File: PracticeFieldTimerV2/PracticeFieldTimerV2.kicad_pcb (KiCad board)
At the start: 2 copper layers, 106 x 153 mm, 43 parts, among them J1 External Controls, J3 Panel, J5 /CAN Enable, J6 RJ45-B, J7 RJ45-A, J8 CAN Terminate, U1 ESP32-DevKitC, U2 PCF8574N, U3 20 x 4 LCD, U4 DS3231MZ_TRL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

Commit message: Fix reversed power and ground on LCD backlight LED.
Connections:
- U3 pad 15: GND -> +3.3V
- U3 pad 16: +3.3V -> GND
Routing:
- net +3.3V: track 282.1 -> 283.4 mm
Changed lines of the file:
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@@
 			)
 		)
-		(fp_text user "GPIO33"
-			(at 1.27 17.78 90)
-			(unlocked yes)
-			(layer "F.SilkS")
-			(effects
-				(font
-					(size 0.8 0.7)
-					(thickness 0.15)
-				)
-				(justify left)
-			)
-		)
 		(fp_text user "GPIO34"
 			(at 1.27 10.16 90)
@@
 			(layers "*.Cu" "*.Mask")
 			(remove_unused_layers no)
-			(net 2 "GND")
-			(pinfunction "LED-")
+			(net 1 "+3.3V")
+			(pinfunction "A")
 			(pintype "power_in")
 		)
@@
 			(layers "*.Cu" "*.Mask")
 			(remove_unused_layers no)
-			(net 1 "+3.3V")
-			(pinfunction "LED+")
+			(net 2 "GND")
+			(pinfunction "K")
 			(pintype "passive")
 		)
@@
 	)
 	(segment
+		(start 56.932088 62.559317)
+		(end 56.932088 64.547963)
+		(width 0.4)
+		(layer "F.Cu")
+		(net 1)
+	)
+	(segment
 		(start 126.43 53.28)
 		(end 129.6 53.28)
@@
 	)
 	(segment
-		(start 56.932088 62.559317)
-		(end 56.932088 64.547963)
+		(start 90.39 47.95)
+		(end 90.64 47.95)
+		(width 0.2)
+		(layer "F.Cu")
+		(net 1)
+	)
+	(segment
+		(start 90.39 47.95)
+		(end 89.96 47.95)
 		(width 0.4)
 		(layer "F.Cu")
@@
 	)
 	(segment
-		(start 47.77 47.96)
-		(end 45.76 49.97)
+		(start 89.95 47.96)
+		(end 47.77 47.96)
 		(width 0.4)
 		(layer "F.Cu")
@@
 	)
 	(segment
+		(start 89.96 47.95)
+		(end 89.95 47.96)
+		(width 0.4)
+		(layer "F.Cu")
+		(net 1)
+	)
+	(segment
 		(start 50.4188 150.51)
 		(end 50.4088 150.52)
@@
 	)
 	(segment
-		(start 126.4 53.31)
-		(end 126.43 53.28)
-		(width 0.2)
-		(layer "F.Cu")
-		(net 1)
-	)
-	(segment
-		(start 92.992088 47.96)
-		(end 47.77 47.96)
-		(width 0.4)
-		(layer "F.Cu")
-		(net 1)
-	)
-	(segment
-		(start 93.022088 47.99)
-		(end 121.08 47.99)
-		(width 0.2)
-		(layer "F.Cu")
-		(net 1)
-	)
-	(segment
 		(start 121.08 47.99)
 		(end 126.4 53.31)
@@
 	)
 	(segment
+		(start 90.64 47.95)
+		(end 90.68 47.99)
+		(width 0.2)
+		(layer "F.Cu")
+		(net 1)
+	)
+	(segment
 		(start 47.73 61.11)
 		(end 48.14 61.11)
@@
 	)
 	(segment
-		(start 93.002088 47.97)
-		(end 93.022088 47.99)
+		(start 126.4 53.31)
+		(end 126.43 53.28)
+		(width 0.2)
+		(layer "F.Cu")
+		(net 1)
+	)
+	(segment
+		(start 90.64 47.95)
+		(end 90.65 47.96)
 		(width 0.2)
 		(layer "F.Cu")
@@
 	)
 	(segment
-		(start 93.022088 47.99)
-		(end 92.992088 47.96)
-		(width 0.4)
+		(start 90.68 47.99)
+		(end 121.08 47.99)
+		(width 0.2)
 		(layer "F.Cu")
 		(net 1)
@@
 		(net 1)
 	)
+	(segment
+		(start 47.77 47.96)
+		(end 45.76 49.97)
+		(width 0.4)
+		(layer "F.Cu")
+		(net 1)
+	)
 	(via
 		(at 47.73 61.11)
@@
 	)
 	(via
-		(at 93.022088 47.99)
+		(at 90.39 47.95)
 		(size 0.9)
 		(drill 0.3)
@@
 	)
 	(segment
-		(start 93.022088 47.99)
-		(end 93.022088 52.397963)
+		(start 47.73 58.882907)
+		(end 46.851 58.003907)
 		(width 0.4)
 		(layer "B.Cu")
@@
 	)
 	(segment
-		(start 47.73 58.882907)
-		(end 46.851 58.003907)
-		(width 0.4)
+		(start 89.952088 60.717912)
+		(end 89.952088 64.547963)
+		(width 0.2)
 		(layer "B.Cu")
 		(net 1)
@@
 	)
 	(segment
-		(start 92.542088 55.597963)
-		(end 92.522928 55.617123)
-		(width 0.4)
-		(layer "B.Cu")
-		(net 1)
-	)
-	(segment
 		(start 47.73 113.95)
 		(end 49.35 113.95)
@@
 	)
 	(segment
-		(start 92.522928 55.617123)
-		(end 92.522928 63.297383)
+		(start 45.85 46.08)
+		(end 45.85 38.62)
 		(width 0.4)
 		(layer "B.Cu")
@@
 	)
 	(segment
-		(start 45.85 46.08)
-		(end 45.85 38.62)
-		(width 0.4)
+		(start 90.39 60.22)
+		(end 90.42 60.25)
+		(width 0.2)
 		(layer "B.Cu")
 		(net 1)
 	)
 	(segment
-		(start 93.022088 52.397963)
-		(end 92.542088 52.877963)
-		(width 0.4)
+		(start 90.42 60.25)
+		(end 89.952088 60.717912)
+		(width 0.2)
 		(layer "B.Cu")
 		(net 1)
 	)
 	(segment
-		(start 92.542088 52.877963)
-		(end 92.542088 55.597963)
-		(width 0.4)
+		(start 90.39 47.95)
+		(end 90.39 60.22)
+		(width 0.2)
 		(layer "B.Cu")
 		(net 1)

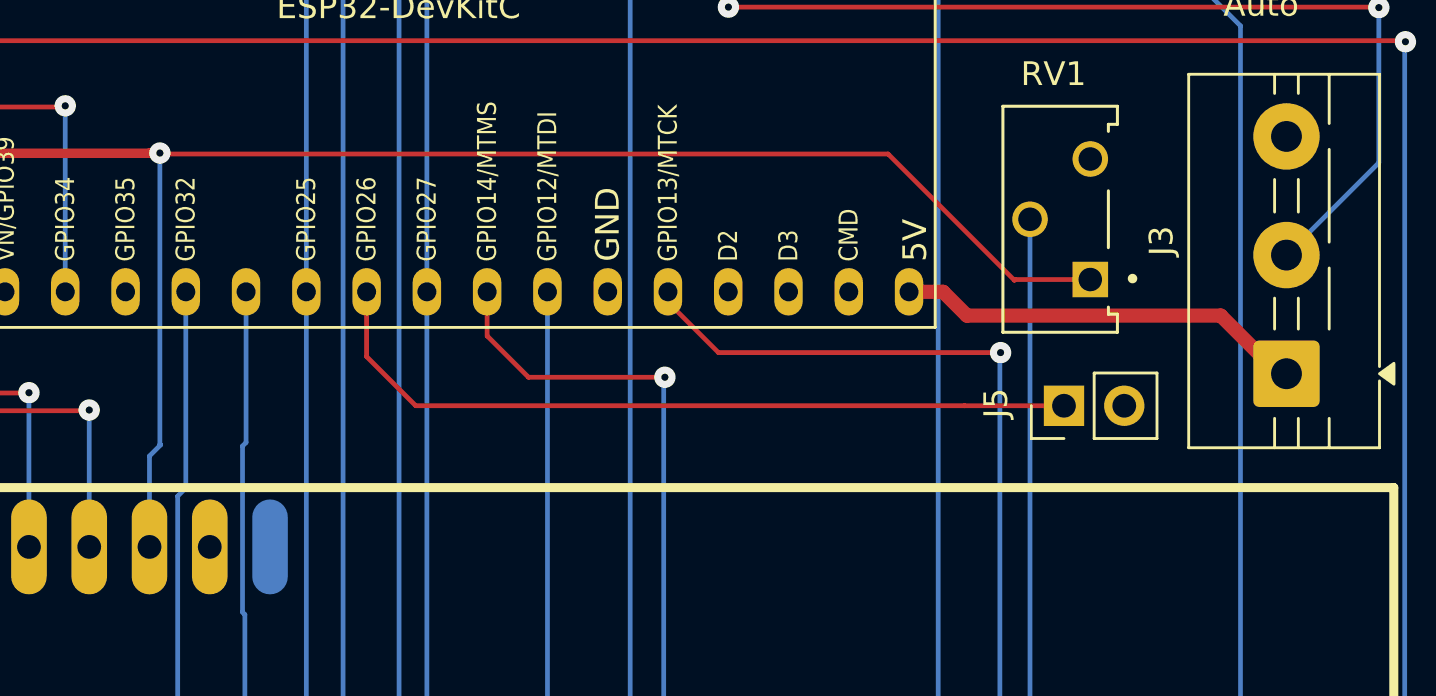
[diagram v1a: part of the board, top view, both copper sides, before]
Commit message: Power the LCD backlight from +5 to minimize load on the ESP32 voltage reducer and for maximum brightness.
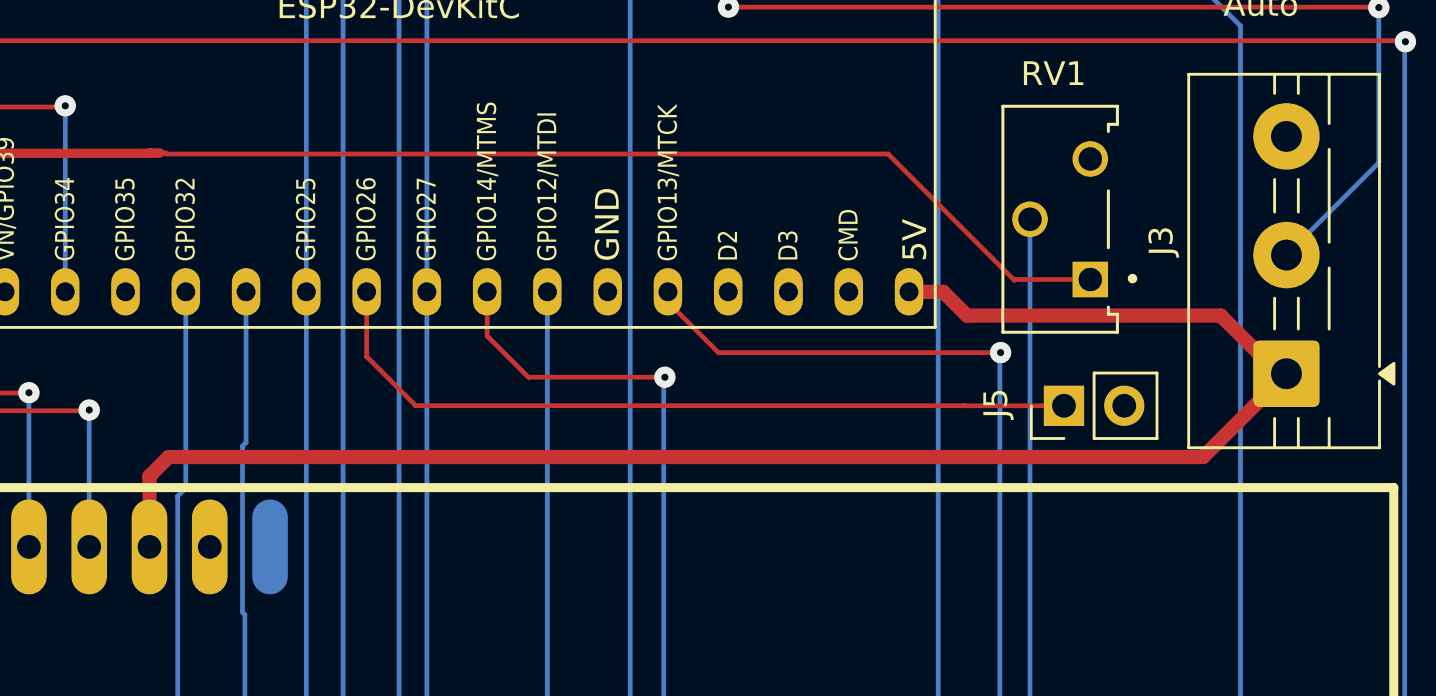
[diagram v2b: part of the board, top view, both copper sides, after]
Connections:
- U3 pad 15: +3.3V -> +5V
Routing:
- net +5V: track 17.9 -> 70.3 mm
- net +3.3V: track 283.4 -> 266.6 mm, vias 3 -> 2
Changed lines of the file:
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@@
 			(layers "*.Cu" "*.Mask")
 			(remove_unused_layers no)
-			(net 1 "+3.3V")
+			(net 13 "+5V")
 			(pinfunction "A")
 			(pintype "power_in")
@@
 		(net 1)
 	)
-	(via
-		(at 90.39 47.95)
-		(size 0.9)
-		(drill 0.3)
-		(layers "F.Cu" "B.Cu")
-		(net 1)
-	)
 	(segment
 		(start 76.242088 53.797963)
@@
 	)
 	(segment
-		(start 89.952088 60.717912)
-		(end 89.952088 64.547963)
-		(width 0.2)
-		(layer "B.Cu")
-		(net 1)
-	)
-	(segment
 		(start 49.35 113.95)
 		(end 51.38 115.98)
@@
 	)
 	(segment
-		(start 90.39 60.22)
-		(end 90.42 60.25)
-		(width 0.2)
-		(layer "B.Cu")
-		(net 1)
-	)
-	(segment
-		(start 90.42 60.25)
-		(end 89.952088 60.717912)
-		(width 0.2)
-		(layer "B.Cu")
-		(net 1)
-	)
-	(segment
-		(start 90.39 47.95)
-		(end 90.39 60.22)
-		(width 0.2)
-		(layer "B.Cu")
-		(net 1)
-	)
-	(segment
 		(start 46.851 51.061)
 		(end 45.76 49.97)
@@
 	)
 	(segment
-		(start 123.397963 53.797963)
-		(end 121.962088 53.797963)
+		(start 134.3575 60.76)
+		(end 137.8675 57.25)
 		(width 0.6)
 		(layer "F.Cu")
@@
 	)
 	(segment
-		(start 137.8675 57.25)
-		(end 137.55 57.25)
-		(width 0.2)
+		(start 123.397963 53.797963)
+		(end 121.962088 53.797963)
+		(width 0.6)
 		(layer "F.Cu")
 		(net 13)
@@
 	)
 	(segment
+		(start 89.952088 61.567912)
+		(end 90.76 60.76)
+		(width 0.6)
+		(layer "F.Cu")
+		(net 13)
+	)
+	(segment
+		(start 89.952088 64.547963)
+		(end 89.952088 61.567912)
+		(width 0.6)
+		(layer "F.Cu")
+		(net 13)
+	)
+	(segment
 		(start 135.1 54.8)
 		(end 124.4 54.8)
 		(width 0.6)
 		(layer "F.Cu")
+		(net 13)
+	)
+	(segment
+		(start 90.76 60.76)
+		(end 134.3575 60.76)
+		(width 0.6)
+		(layer "F.Cu")

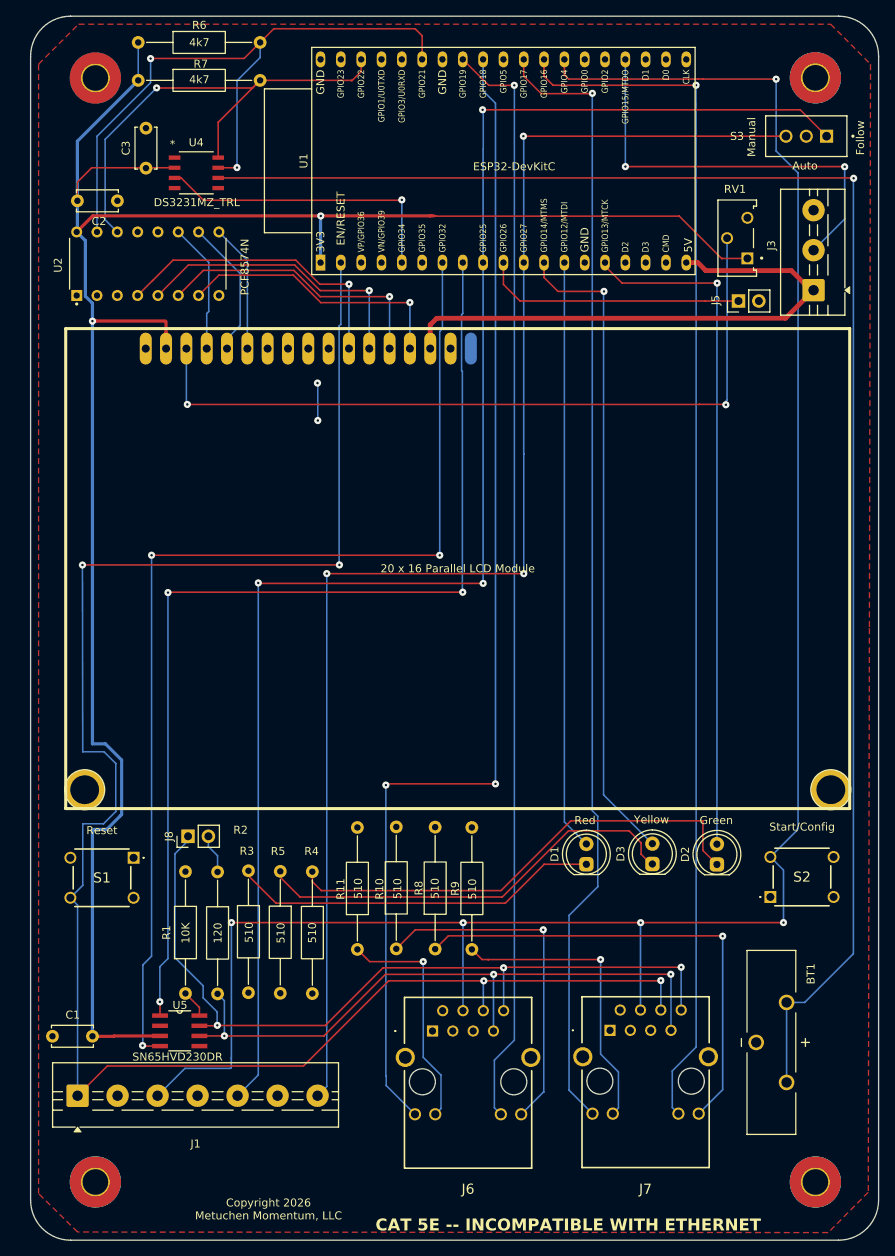
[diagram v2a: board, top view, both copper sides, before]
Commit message: Remove on-board LCD Module and I2C->parallel byte converter. Add terminal strip for off-board display. Shrink the board. The board is still a bit spread out, but the changes are significant enough to commit.
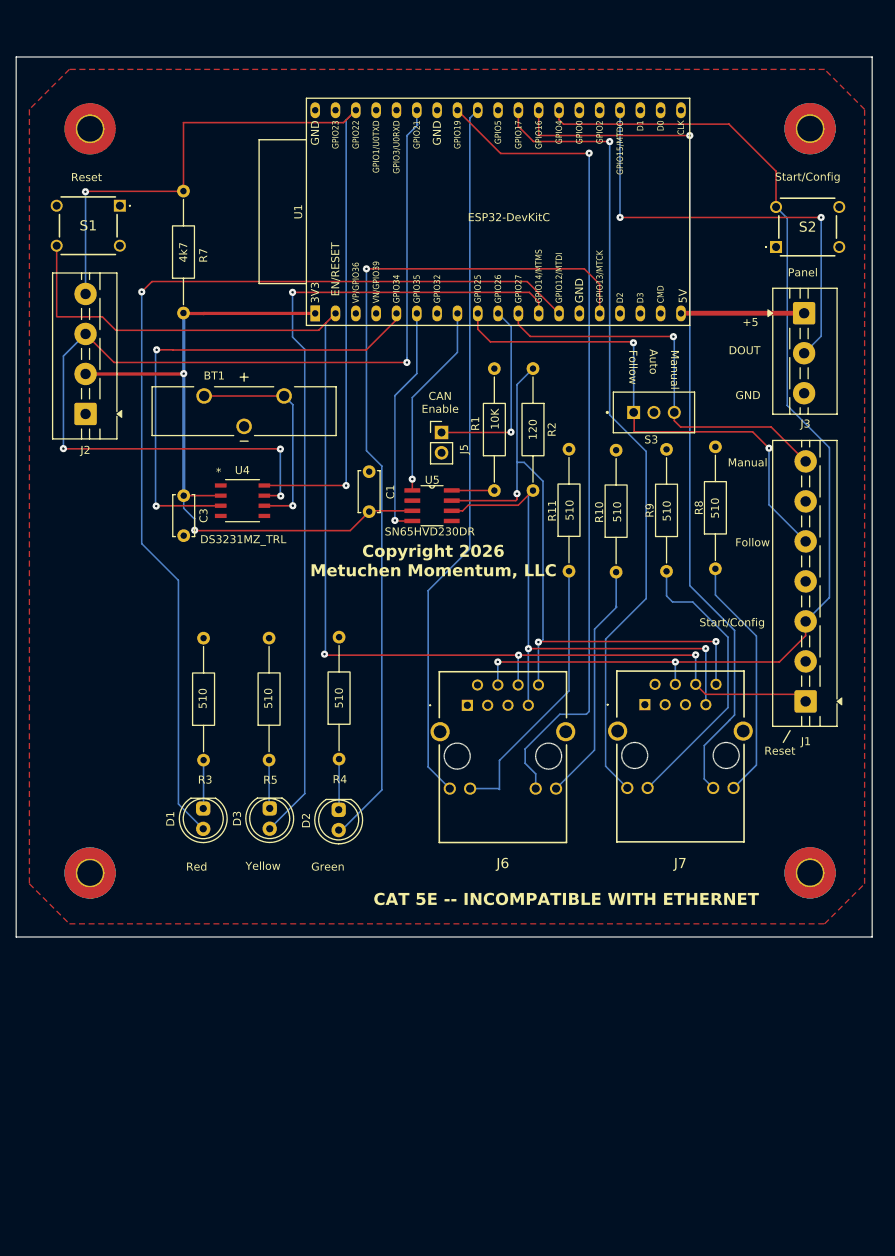
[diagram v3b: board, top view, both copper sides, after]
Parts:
- removed C2: 100n, Capacitor_THT:C_Disc_D5.0mm_W2.5mm_P5.00mm
- removed J8: CAN Terminate, Connector_PinHeader_2.54mm:PinHeader_1x02_P2.54mm_Vertical
- removed R6: 4k7, Resistor_THT:R_Axial_DIN0207_L6.3mm_D2.5mm_P15.24mm_Horizontal
- removed the REF** at (140.0, 119.7)
- removed the REF** at (46.8, 119.7)
- removed RV1: 20K, Misc:TRIM_PV36Y203C01B00
- removed U2: PCF8574N, Misc:PCF8574N
- removed U3: 20 x 4 LCD, Misc:LCD-20x4-parallel
- added J2: Screw_Terminal_01x04, TerminalBlock:TerminalBlock_MaiXu_MX126-5.0-04P_1x04_P5.00mm, F.Cu at (46.9, 72.7)
- moved J1 103.5 mm to (136.9, 108.7), turned to 90 degrees
- moved BT1 102.8 mm to (66.7, 72.4), turned to 0 degrees
- moved S1 81.5 mm to (51.2, 46.7)
- moved S2 81.3 mm to (133.2, 51.9)
- moved R2 74.3 mm to (102.8, 67.0)
- moved C1 74.1 mm to (82.3, 84.9), turned to 90 degrees
- moved R1 73.8 mm to (98.0, 82.3)
- moved U5 72.8 mm to (90.2, 84.2)
- moved R8 59.1 mm to (125.6, 92.1)
- moved R10 54.5 mm to (113.2, 92.5)
- moved R11 54.2 mm to (107.3, 92.4)
- moved R9 53.2 mm to (119.5, 92.4)
- moved D1 48.4 mm to (61.6, 122.0), turned to -90 degrees
- moved D3 48.3 mm to (69.9, 122.0), turned to -90 degrees
- moved D2 47.8 mm to (78.5, 122.2), turned to -90 degrees
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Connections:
- R2 pad 1: Net-(J8-Pin_2) -> CANH
- U1 pad 6: unconnected-(U1-VDET_2/GPIO35/ADC1_CH7-Pad6) -> CAN RX
- U1 pad 7: CAN RX -> unconnected-(U1-32K_XP/GPIO32/ADC1_CH4-Pad7)
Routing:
- net +3.3V: track 266.6 -> 89.3 mm
- net Net-(U4-VBAT): track 197.3 -> 27.7 mm
- net /Follow: track 196.8 -> 64.6 mm, vias 3 -> 2
- net /Manual: track 178.2 -> 50.5 mm, vias 3 -> 1
- net /CFG-START: track 257.0 -> 138.6 mm, vias 5 -> 2
- net CAN RX: track 136.7 -> 29.2 mm, vias 3 -> 1
- net CAN TX: track 131.5 -> 24.5 mm, vias 3 -> 1
- net Net-(U3-V0): track 95.3 -> 0.00 mm, vias 2 -> 0
- net /RST: track 231.1 -> 155.7 mm, vias 4 -> 3
- net /RJ45-B-Yellow: track 147.6 -> 88.4 mm, vias 2 -> 0
- net +5V: track 70.3 -> 15.4 mm
- net Net-(D2-K): track 60.4 -> 6.03 mm
- net I2C SCL: track 61.1 -> 113.5 mm, vias 1 -> 2
- net Net-(D1-A): track 73.8 -> 124.7 mm, vias 0 -> 1
- net Net-(D3-K): track 54.5 -> 5.96 mm
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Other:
- board size 106 x 153 mm -> 107 x 110 mm
- board text added: "+5"
- board text added: "120"
- board text added: "4k7"
- board text added: "CAN Enable"
- board text added: "DOUT"
- board text added: "GND"
- board text added: "Panel"
- board text added: "← 93mm →"
- board text removed: "← 138mm →"

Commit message: Finish shrinking the board. Could do more, but the benefit doesn't justify the effort.
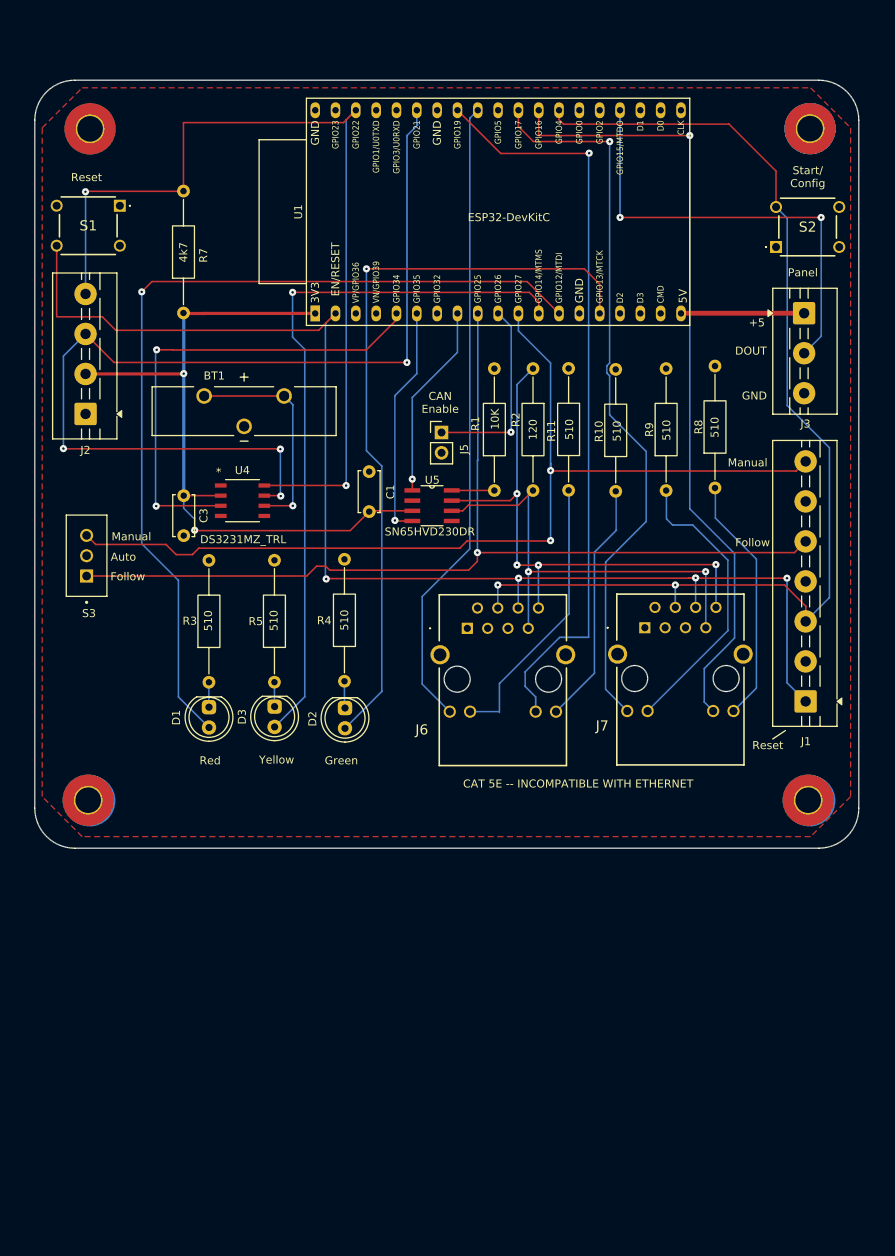
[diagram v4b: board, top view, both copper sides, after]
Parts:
- removed G***: LOGO, Misc:MetuchenMomentumLogo90Percent
- added Logo80%: LOGO, Misc:MetuchenMomentumLogo80Percent, B.Cu at (92.1, 70.4)
- moved S3 73.1 mm to (47.0, 90.4), turned to 90 degrees
- moved D2 12.7 mm to (79.3, 109.5)
- moved D3 12.7 mm to (70.5, 109.3)
- moved D1 12.7 mm to (62.3, 109.4)
- moved R11 10.1 mm to (107.2, 82.3)
- moved R10 10.1 mm to (113.1, 82.4)
- moved R8 10.1 mm to (125.5, 82.0)
- moved R9 10.1 mm to (119.4, 82.3)
- moved R4 9.75 mm to (79.2, 106.1)
- moved R5 9.75 mm to (70.5, 106.2)
- moved R3 9.75 mm to (62.3, 106.3)
- moved J6 9.62 mm to (94.6, 99.5)
- moved J7 9.62 mm to (116.8, 99.4)
- moved REF** 9.11 mm to (47.2, 121.0)
- moved REF** 9.08 mm to (137.2, 121.0)
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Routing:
- net /Manual: track 50.5 -> 122.7 mm, vias 1 -> 2
- net /Follow: track 64.6 -> 122.6 mm, vias 2 -> 1
- net CANH: track 83.1 -> 69.6 mm, vias 3 -> 4
- net Net-(D3-A): track 102.2 -> 89.2 mm
- net Net-(D2-A): track 106.7 -> 93.8 mm
- net Net-(D1-A): track 124.7 -> 112.3 mm
- net CANL: track 67.5 -> 57.8 mm
- net /RJ45-A-Green: track 107.9 -> 98.4 mm
- net /RJ45-B-Green: track 104.0 -> 94.5 mm
- net /RJ45-A-Yellow: track 100.1 -> 90.8 mm
- net /RJ45-B-Yellow: track 88.4 -> 79.4 mm
- net /RST: track 155.7 -> 161.3 mm, vias 3 -> 4
- net Net-(D3-K): track 5.96 -> 3.03 mm
- net Net-(D1-K): track 6.01 -> 3.10 mm
- net Net-(D2-K): track 6.03 -> 3.28 mm
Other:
- board size 107 x 110 mm -> 103 x 96 mm
- board text added: "Start/ Config"
- board text added: "← 84mm → center to center"
- board text added: "← 90mm center to center →"
- board text removed: "Copyright 2026 Metuchen Momentum, LLC"
- board text removed: "Start/Config"
- board text removed: "← 90mm →"
- board text removed: "← 93mm →"
